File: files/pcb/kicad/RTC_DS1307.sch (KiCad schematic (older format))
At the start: 8 parts, among them IC11 DS1307, X2 32.768kHz

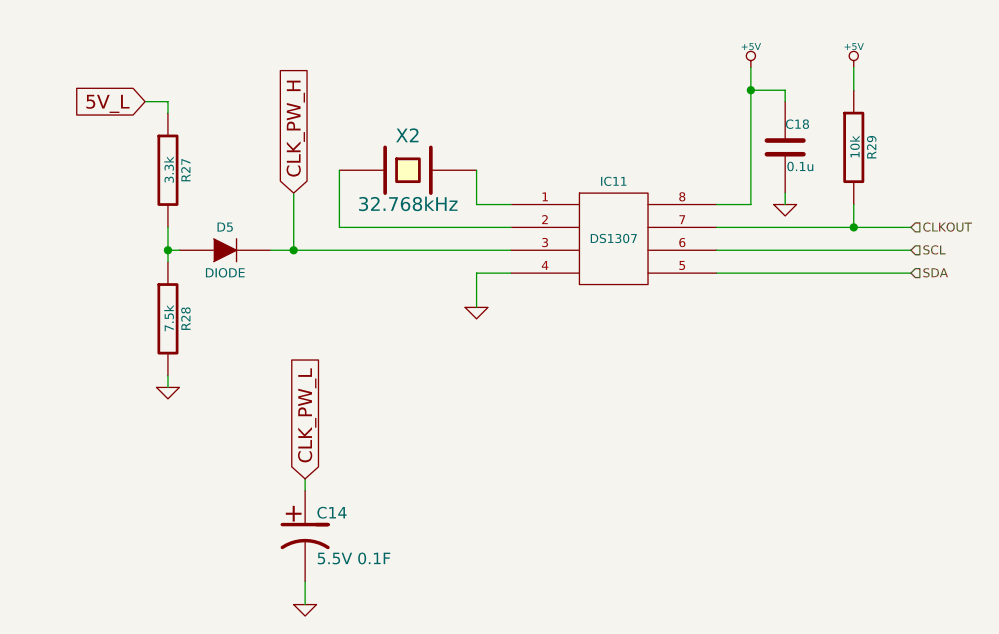
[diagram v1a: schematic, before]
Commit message: 設計見直し
部品見直し
USB・DCジャック自動切り替え
マイコンを下段のボードに移動
ニキシー管駆動電源を上段ボードに移動
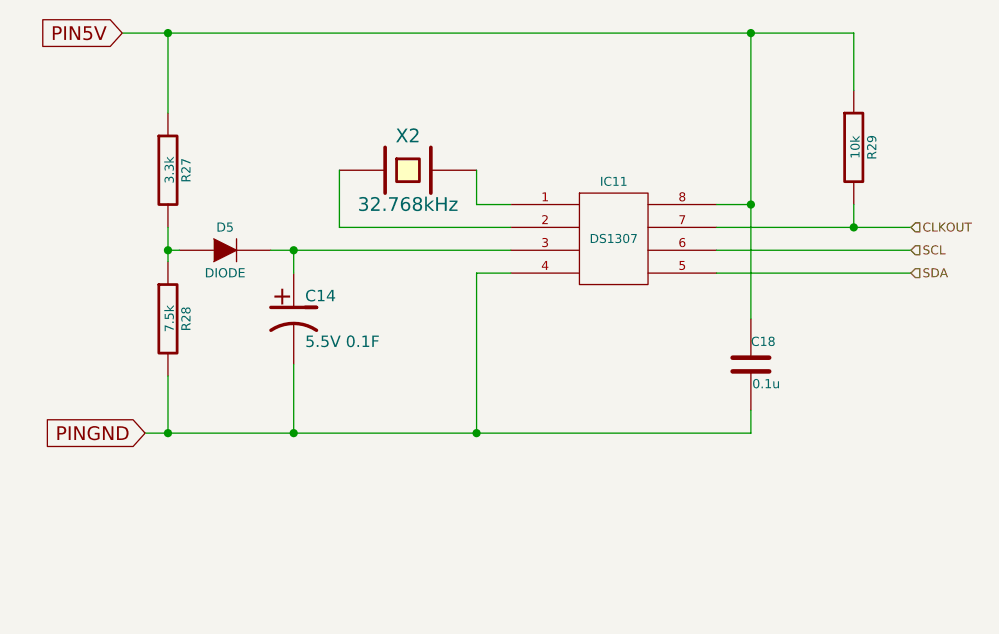
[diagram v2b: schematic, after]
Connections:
- net 5V_L is gone; now on net PIN5V: R27.1
- net CLK_PW_L is gone; now on an unnamed net: C14.1
- net +5V renamed PIN5V
- net CLK_PW_H: no longer names the net of D5.2 (K), IC11.3
- net GND renamed PINGND
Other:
- moved on the sheet: C14, C18
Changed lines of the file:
@@
 $Descr A4 11693 8268
 encoding utf-8
-Sheet 10 11
+Sheet 8 8
 Title ""
-Date "31 aug 2014"
+Date "1 sep 2014"
 Rev ""
 Comp ""
@@
 L CP1 C14
 U 1 1 53F95FE8
-P 4750 5450
-F 0 "C14" H 4800 5550 50  0000 L CNN
-F 1 "5.5V 0.1F" H 4800 5350 50  0000 L CNN
-F 2 "~" H 4750 5450 60  0000 C CNN
-F 3 "~" H 4750 5450 60  0000 C CNN
-	1    4750 5450
+P 4700 4500
+F 0 "C14" H 4750 4600 50  0000 L CNN
+F 1 "5.5V 0.1F" H 4750 4400 50  0000 L CNN
+F 2 "~" H 4700 4500 60  0000 C CNN
+F 3 "~" H 4700 4500 60  0000 C CNN
+	1    4700 4500
 	1    0    0    -1
 $EndComp
@@
 	1    0    0    -1
 $EndComp
-$Comp
-L GND #PWR043
-U 1 1 53F96055
-P 4150 4800
-F 0 "#PWR043" H 4150 4800 30  0001 C CNN
-F 1 "GND" H 4150 4730 30  0001 C CNN
-F 2 "" H 4150 4800 60  0000 C CNN
-F 3 "" H 4150 4800 60  0000 C CNN
-	1    4150 4800
-	1    0    0    -1
-$EndComp
 Wire Wire Line
 	5650 4000 5500 4000
@@
 	4900 4100 4900 3850
 Wire Wire Line
-	4150 4750 4150 4800
-Wire Wire Line
 	6700 4000 6550 4000
 Wire Wire Line
-	6700 3400 6700 4000
+	6700 3250 6700 4500
 Wire Wire Line
 	6550 4100 7400 4100
@@
 Wire Wire Line
 	6550 4300 7400 4300
-$Comp
-L +5V #PWR044
-U 1 1 53F961EF
-P 6700 3400
-F 0 "#PWR044" H 6700 3490 20  0001 C CNN
-F 1 "+5V" H 6700 3490 30  0000 C CNN
-F 2 "" H 6700 3400 60  0000 C CNN
-F 3 "" H 6700 3400 60  0000 C CNN
-	1    6700 3400
-	1    0    0    -1
-$EndComp
-$Comp
-L GND #PWR045
-U 1 1 53F961FF
-P 5500 4450
-F 0 "#PWR045" H 5500 4450 30  0001 C CNN
-F 1 "GND" H 5500 4380 30  0001 C CNN
-F 2 "" H 5500 4450 60  0000 C CNN
-F 3 "" H 5500 4450 60  0000 C CNN
-	1    5500 4450
-	1    0    0    -1
-$EndComp
 Wire Wire Line
 	5650 4300 5500 4300
 Wire Wire Line
-	5500 4300 5500 4450
+	5500 4300 5500 5000
 Wire Wire Line
-	7150 3400 7150 3500
-$Comp
-L +5V #PWR046
-U 1 1 53F96268
-P 7150 3400
-F 0 "#PWR046" H 7150 3490 20  0001 C CNN
-F 1 "+5V" H 7150 3490 30  0000 C CNN
-F 2 "" H 7150 3400 60  0000 C CNN
-F 3 "" H 7150 3400 60  0000 C CNN
-	1    7150 3400
-	1    0    0    -1
-$EndComp
+	7150 3250 7150 3500
 Wire Wire Line
 	5500 4000 5500 3850
@@
 	4200 4200 4150 4200
 Connection ~ 4150 4200
+Wire Wire Line
+	4700 5000 4700 4700
 $Comp
-L GND #PWR047
-U 1 1 53FA2AE8
-P 4750 5750
-F 0 "#PWR047" H 4750 5750 30  0001 C CNN
-F 1 "GND" H 4750 5680 30  0001 C CNN
-F 2 "" H 4750 5750 60  0000 C CNN
-F 3 "" H 4750 5750 60  0000 C CNN
-	1    4750 5750
+L C C18
+U 1 1 53FF68E6
+P 6700 4700
+F 0 "C18" H 6700 4800 40  0000 L CNN
+F 1 "0.1u" H 6706 4615 40  0000 L CNN
+F 2 "~" H 6738 4550 30  0000 C CNN
+F 3 "~" H 6700 4700 60  0000 C CNN
+	1    6700 4700
 	1    0    0    -1
 $EndComp
 Wire Wire Line
-	4750 5650 4750 5750
-$Comp
-L C C18
-U 1 1 53FF68E6
-P 6850 3750
-F 0 "C18" H 6850 3850 40  0000 L CNN
-F 1 "0.1u" H 6856 3665 40  0000 L CNN
-F 2 "~" H 6888 3600 30  0000 C CNN
-F 3 "~" H 6850 3750 60  0000 C CNN
-	1    6850 3750
-	1    0    0    -1
-$EndComp
-$Comp
-L GND #PWR048
-U 1 1 53FF68F8
-P 6850 4000
-F 0 "#PWR048" H 6850 4000 30  0001 C CNN
-F 1 "GND" H 6850 3930 30  0001 C CNN
-F 2 "" H 6850 4000 60  0000 C CNN
-F 3 "" H 6850 4000 60  0000 C CNN
-	1    6850 4000
-	1    0    0    -1
-$EndComp
+	6700 5000 6700 4900
 Wire Wire Line
-	6850 4000 6850 3950
+	3950 3250 7150 3250
 Wire Wire Line
-	6850 3550 6850 3500
+	4150 3250 4150 3600
 Wire Wire Line
-	6850 3500 6700 3500
-Connection ~ 6700 3500
-Text GLabel 4050 3550 0    60   Input ~ 0
-5V_L
-Wire Wire Line
-	4050 3550 4150 3550
-Wire Wire Line
-	4150 3550 4150 3600
-Text GLabel 4700 3950 1    60   Input ~ 0
-CLK_PW_H
-Text GLabel 4750 5200 1    60   Input ~ 0
-CLK_PW_L
-Wire Wire Line
-	4750 5250 4750 5200
+	4700 4300 4700 4200
 Wire Wire Line
 	4600 4200 5650 4200
+Connection ~ 4700 4200
+Text GLabel 4050 5000 0    60   Input ~ 0
+PINGND
+Text GLabel 3950 3250 0    60   Input ~ 0
+PIN5V
 Wire Wire Line
-	4700 4200 4700 3950
-Connection ~ 4700 4200
+	4150 4750 4150 5000
+Wire Wire Line
+	4050 5000 6700 5000
+Connection ~ 4150 5000
+Connection ~ 4700 5000
+Connection ~ 4150 3250
+Connection ~ 6700 3250
+Connection ~ 5500 5000
+Connection ~ 6700 4000
 $EndSCHEMATC
